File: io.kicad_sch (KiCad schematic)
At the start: 1 part, among them U201 xc7z010clg400

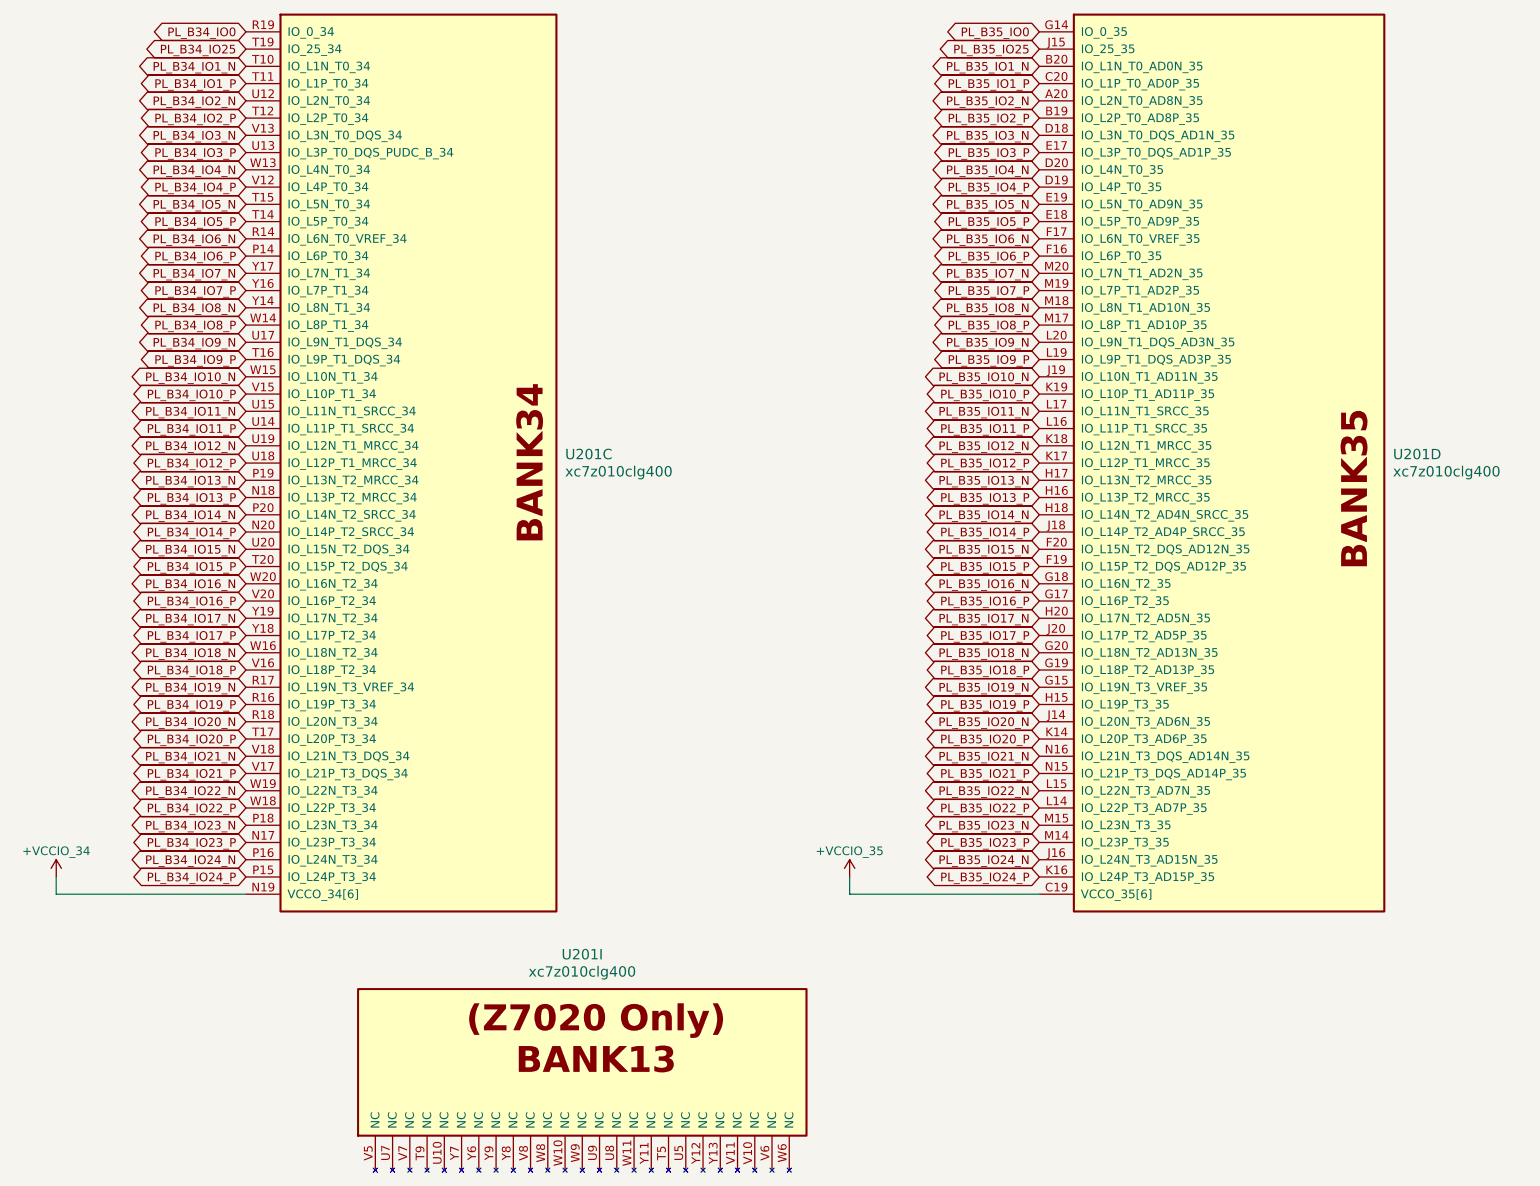
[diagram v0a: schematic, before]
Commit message: layout: before rerouting ddr
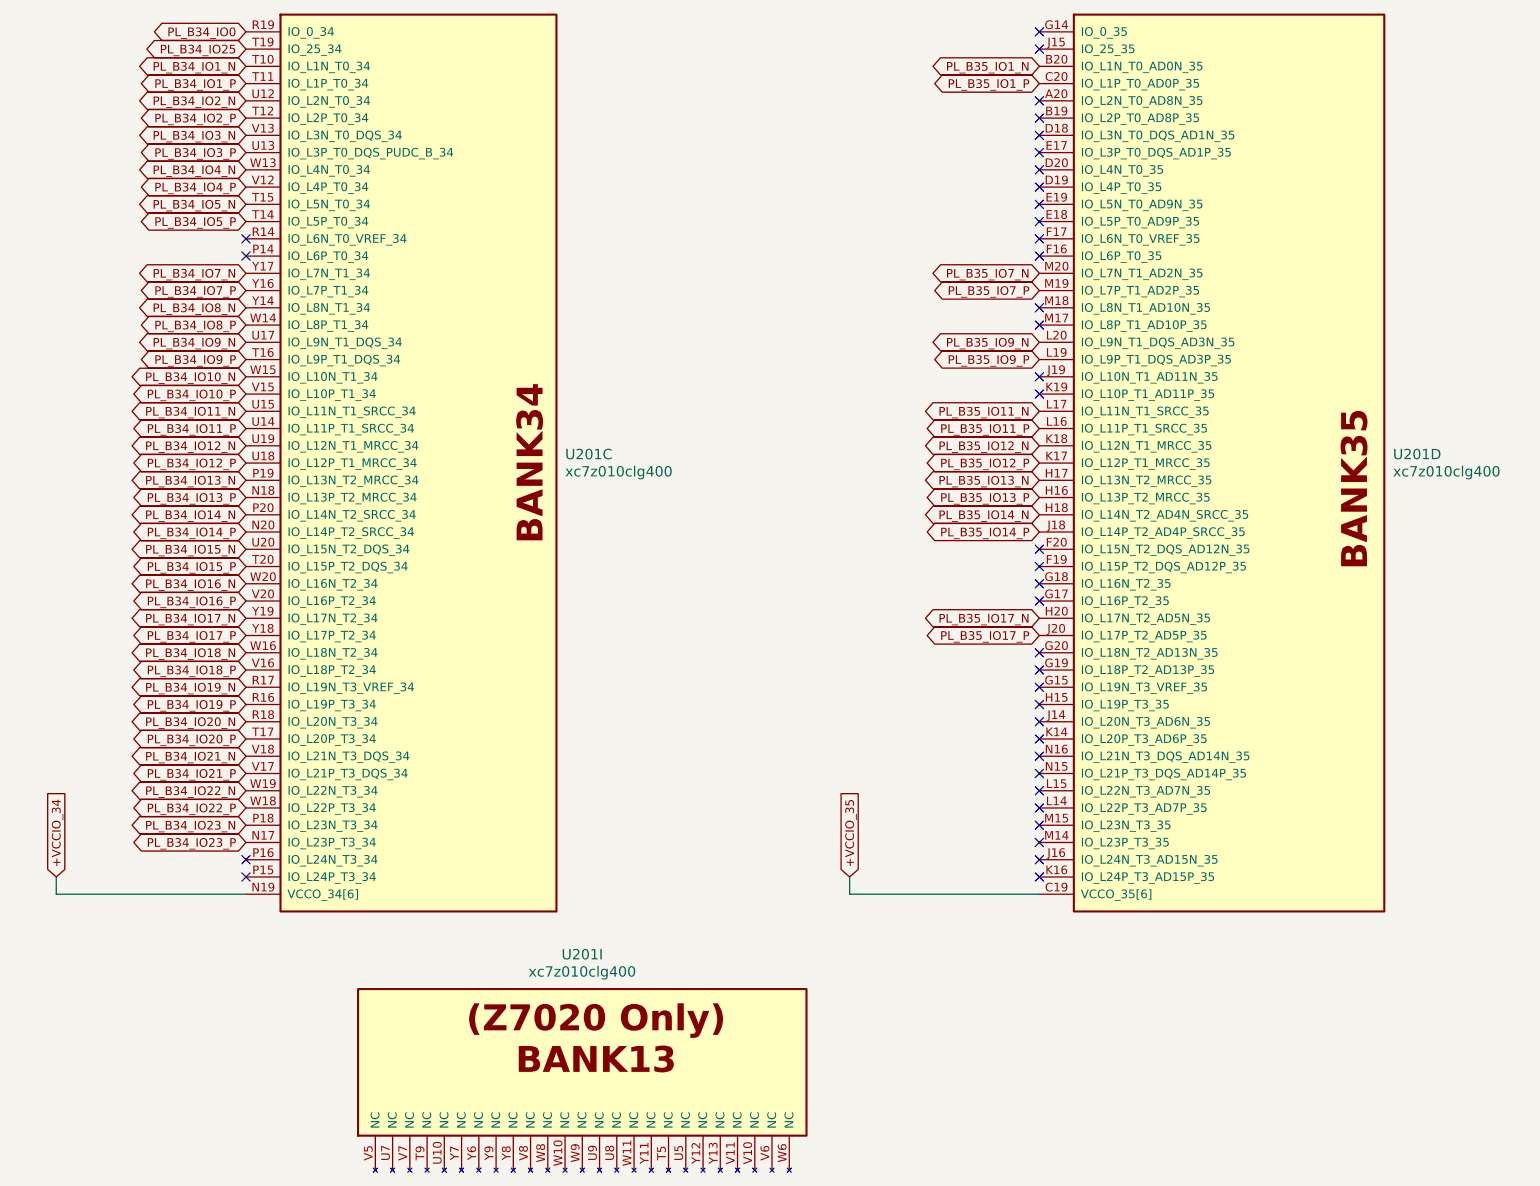
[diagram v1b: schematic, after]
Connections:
- net PL_B34_IO24_N: no longer names the net of U201.P16 (IO_L24N_T3_34)
- net PL_B34_IO24_P: no longer names the net of U201.P15 (IO_L24P_T3_34)
- net PL_B34_IO6_N: no longer names the net of U201.R14 (IO_L6N_T0_VREF_34)
- net PL_B34_IO6_P: no longer names the net of U201.P14 (IO_L6P_T0_34)
- net PL_B35_IO0: no longer names the net of U201.G14 (IO_0_35)
- net PL_B35_IO10_N: no longer names the net of U201.J19 (IO_L10N_T1_AD11N_35)
- net PL_B35_IO10_P: no longer names the net of U201.K19 (IO_L10P_T1_AD11P_35)
- net PL_B35_IO15_N: no longer names the net of U201.F20 (IO_L15N_T2_DQS_AD12N_35)
- net PL_B35_IO15_P: no longer names the net of U201.F19 (IO_L15P_T2_DQS_AD12P_35)
- net PL_B35_IO16_N: no longer names the net of U201.G18 (IO_L16N_T2_35)
- net PL_B35_IO16_P: no longer names the net of U201.G17 (IO_L16P_T2_35)
- net PL_B35_IO18_N: no longer names the net of U201.G20 (IO_L18N_T2_AD13N_35)
- net PL_B35_IO18_P: no longer names the net of U201.G19 (IO_L18P_T2_AD13P_35)
- net PL_B35_IO19_N: no longer names the net of U201.G15 (IO_L19N_T3_VREF_35)
- net PL_B35_IO19_P: no longer names the net of U201.H15 (IO_L19P_T3_35)
- net PL_B35_IO20_N: no longer names the net of U201.J14 (IO_L20N_T3_AD6N_35)
- net PL_B35_IO20_P: no longer names the net of U201.K14 (IO_L20P_T3_AD6P_35)
- net PL_B35_IO21_N: no longer names the net of U201.N16 (IO_L21N_T3_DQS_AD14N_35)
- net PL_B35_IO21_P: no longer names the net of U201.N15 (IO_L21P_T3_DQS_AD14P_35)
- net PL_B35_IO22_N: no longer names the net of U201.L15 (IO_L22N_T3_AD7N_35)
- net PL_B35_IO22_P: no longer names the net of U201.L14 (IO_L22P_T3_AD7P_35)
- net PL_B35_IO23_N: no longer names the net of U201.M15 (IO_L23N_T3_35)
- net PL_B35_IO23_P: no longer names the net of U201.M14 (IO_L23P_T3_35)
- net PL_B35_IO24_N: no longer names the net of U201.J16 (IO_L24N_T3_AD15N_35)
- net PL_B35_IO24_P: no longer names the net of U201.K16 (IO_L24P_T3_AD15P_35)
- net PL_B35_IO25: no longer names the net of U201.J15 (IO_25_35)
- net PL_B35_IO2_N: no longer names the net of U201.A20 (IO_L2N_T0_AD8N_35)
- net PL_B35_IO2_P: no longer names the net of U201.B19 (IO_L2P_T0_AD8P_35)
- net PL_B35_IO3_N: no longer names the net of U201.D18 (IO_L3N_T0_DQS_AD1N_35)
- net PL_B35_IO3_P: no longer names the net of U201.E17 (IO_L3P_T0_DQS_AD1P_35)
- net PL_B35_IO4_N: no longer names the net of U201.D20 (IO_L4N_T0_35)
- net PL_B35_IO4_P: no longer names the net of U201.D19 (IO_L4P_T0_35)
- net PL_B35_IO5_N: no longer names the net of U201.E19 (IO_L5N_T0_AD9N_35)
- net PL_B35_IO5_P: no longer names the net of U201.E18 (IO_L5P_T0_AD9P_35)
- net PL_B35_IO6_N: no longer names the net of U201.F17 (IO_L6N_T0_VREF_35)
- net PL_B35_IO6_P: no longer names the net of U201.F16 (IO_L6P_T0_35)
- net PL_B35_IO8_N: no longer names the net of U201.M18 (IO_L8N_T1_AD10N_35)
- net PL_B35_IO8_P: no longer names the net of U201.M17 (IO_L8P_T1_AD10P_35)
- no-connect marks 0 -> 38

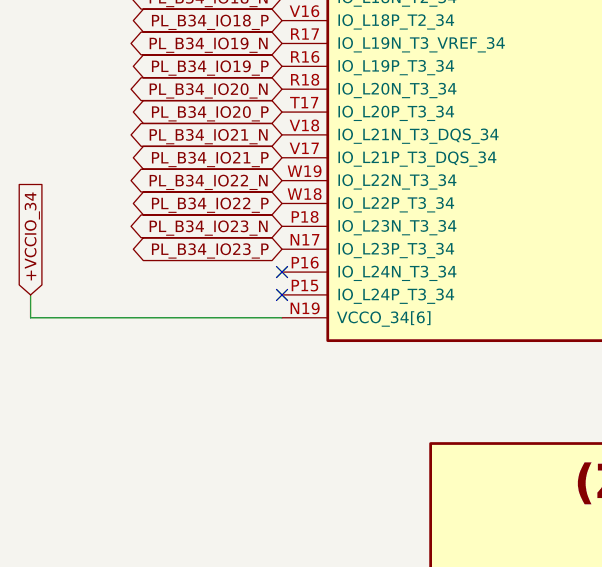
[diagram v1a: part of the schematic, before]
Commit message: layout: add bank 34 pl pair
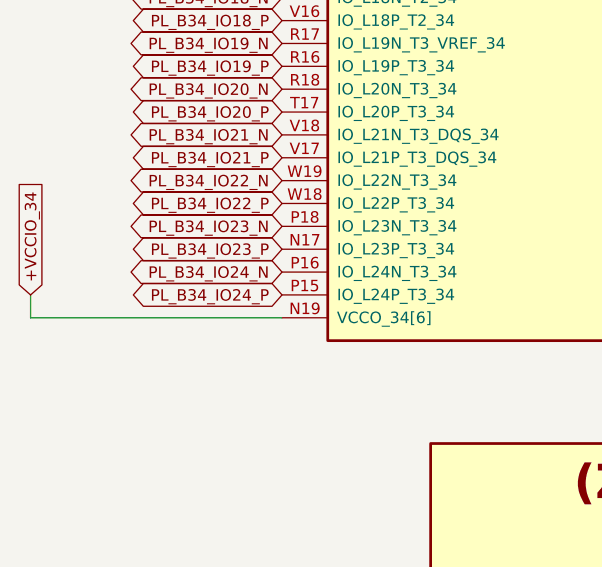
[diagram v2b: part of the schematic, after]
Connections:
- net PL_B34_IO24_P: now reaches U201.P15 (IO_L24P_T3_34)
- net PL_B34_IO24_N: now reaches U201.P16 (IO_L24N_T3_34)
- no-connect marks 38 -> 36
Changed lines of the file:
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@@
 	)
 	(no_connect
-		(at 83.82 144.78)
-	)
-	(no_connect
 		(at 200.66 139.7)
 	)
@@
 	)
 	(no_connect
-		(at 83.82 142.24)
-	)
-	(no_connect
 		(at 200.66 73.66)
 	)
@@
 		)
 	)
+	(global_label "PL_B34_IO24_P"
+		(shape bidirectional)
+		(at 83.82 144.78 180)
+		(effects
+			(font
+				(size 1.27 1.27)
+			)
+			(justify right)
+		)
+		(property "Intersheetrefs" "${INTERSHEET_REFS}"
+			(at 83.82 144.78 0)
+			(hide yes)
+			(show_name no)
+			(do_not_autoplace no)
+			(effects
+				(font
+					(size 1.27 1.27)
+				)
+			)
+		)
+	)
 	(global_label "PL_B34_IO18_N"
 		(shape bidirectional)
@@
 		)
 	)
+	(global_label "PL_B34_IO24_N"
+		(shape bidirectional)
+		(at 83.82 142.24 180)
+		(effects
+			(font
+				(size 1.27 1.27)
+			)
+			(justify right)
+		)
+		(property "Intersheetrefs" "${INTERSHEET_REFS}"
+			(at 83.82 142.24 0)
+			(hide yes)
+			(show_name no)
+			(do_not_autoplace no)
+			(effects
+				(font
+					(size 1.27 1.27)
+				)
+			)
+		)
+	)
 	(global_label "PL_B34_IO19_P"
 		(shape bidirectional)
@@
 			"5a46769d-38fa-4748-8026-c3a0d678ce45" "5e02e99d-f9ab-4284-b908-bd208dfd2947"
 			"6bd1d6db-7e1d-4799-aac4-565e53272c6c" "78ad6370-c3e9-4b66-a231-20ef0d211751"
-			"797c01b0-0e57-49ae-b617-8ec1ba6f2e5a" "7aa4221d-474e-470f-9c05-4256452f8e8a"
-			"82cfa8cd-d805-4a80-b908-da25b46ece87" "8b0ca42c-cb47-470b-92e2-02e37af1b962"
-			"8b3c8865-561e-4ec8-b65a-1bb434446403" "9064db35-f522-44cc-b4cb-e6f569bd0522"
-			"9166ddc3-043e-4aa3-a8a9-5a963f44e3a2" "98f8bd12-81b9-4306-a529-83bad49dd24c"
-			"9b7eb819-549d-4000-9303-bf0309ea660c" "a070e3e7-9bbe-4730-a75c-55775aececb0"
+			"79166ea3-e534-4e9f-8e55-d79f6fd5f340" "797c01b0-0e57-49ae-b617-8ec1ba6f2e5a"
+			"7aa4221d-474e-470f-9c05-4256452f8e8a" "82cfa8cd-d805-4a80-b908-da25b46ece87"
+			"8b0ca42c-cb47-470b-92e2-02e37af1b962" "8b3c8865-561e-4ec8-b65a-1bb434446403"
+			"9064db35-f522-44cc-b4cb-e6f569bd0522" "9166ddc3-043e-4aa3-a8a9-5a963f44e3a2"
+			"98f8bd12-81b9-4306-a529-83bad49dd24c" "9b7eb819-549d-4000-9303-bf0309ea660c"
+			"9d963d73-8776-4d0c-a78a-c54cc73e55ce" "a070e3e7-9bbe-4730-a75c-55775aececb0"
 			"a2267809-b1ae-4e1b-a095-196fd6885eee" "a9519034-0529-4de7-9a35-30e16c7fb695"
 			"b470555d-3a8b-4d45-9e9b-5f826a003767" "b6ae38d1-b64c-4f1e-979a-3b40746ab54f"
